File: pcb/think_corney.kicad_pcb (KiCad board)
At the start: 2 copper layers, 130.3 x 86.5 mm, 112 parts

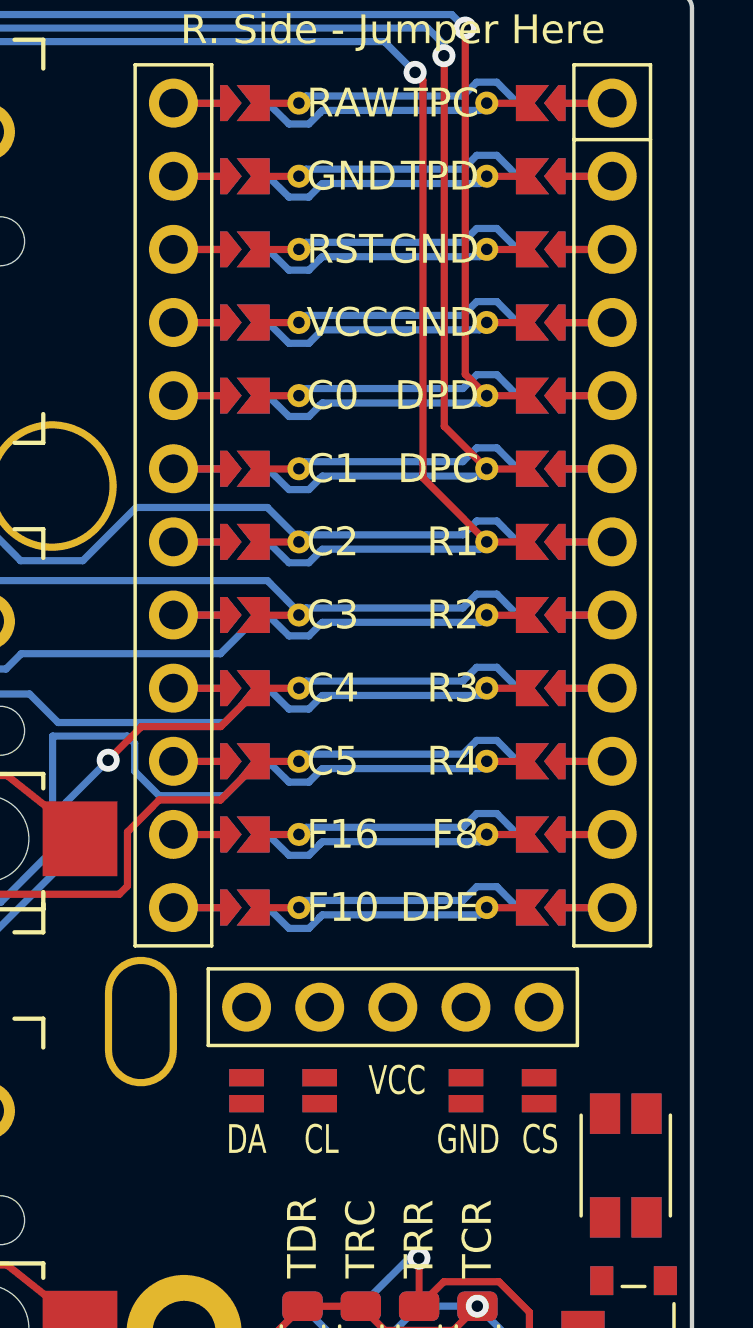
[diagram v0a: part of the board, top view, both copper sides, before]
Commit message: Traces: Added display traces
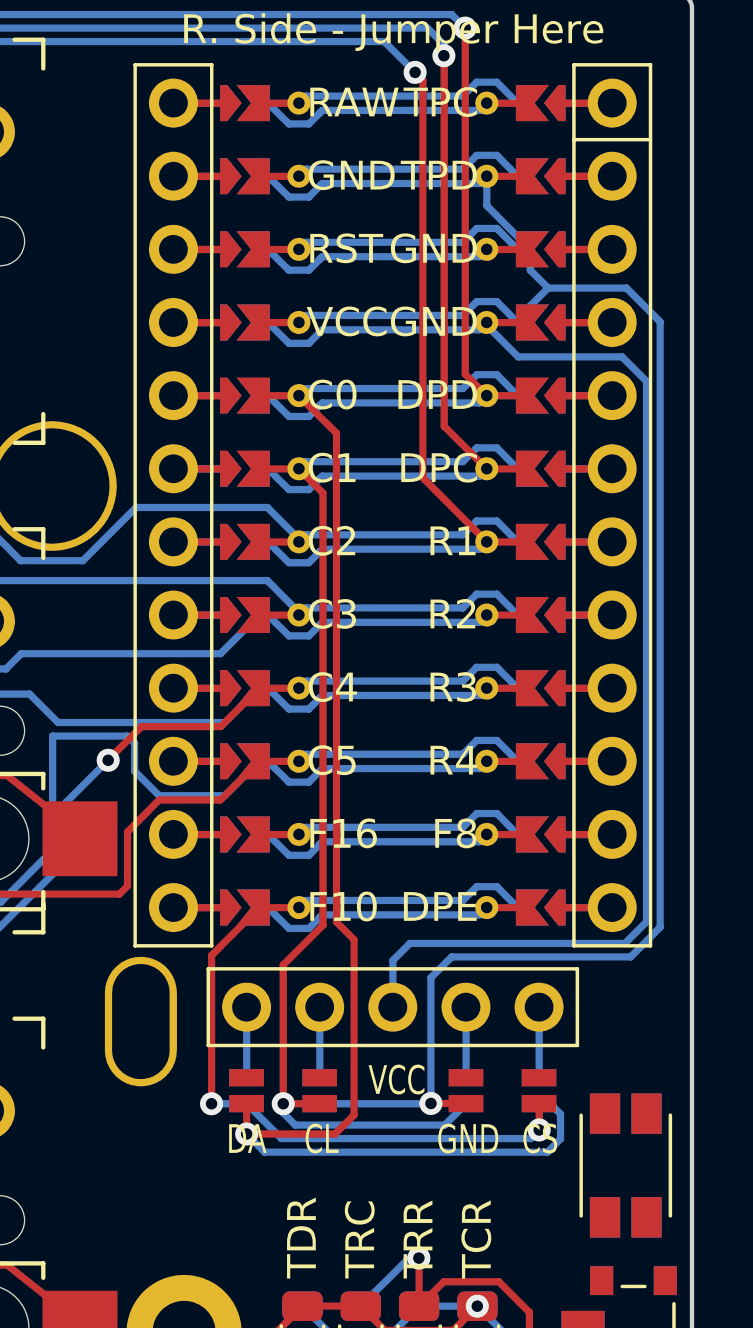
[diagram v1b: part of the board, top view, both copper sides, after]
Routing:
- net GND: track 72.7 -> 122.5 mm, vias 3 -> 4
- net DPD: track 10.2 -> 53.7 mm, vias 0 -> 1
- net VCC: track 45.2 -> 81.3 mm
- net DPC: track 10.2 -> 41.5 mm, vias 0 -> 1
- net DPE: track 10.2 -> 30.4 mm, vias 0 -> 2
- net DISP1_5: track 0.00 -> 2.45 mm
- net DISP1_4: track 0.00 -> 2.45 mm
- net DISP1_2: track 0.00 -> 2.45 mm
- net DISP1_1: track 0.00 -> 2.45 mm

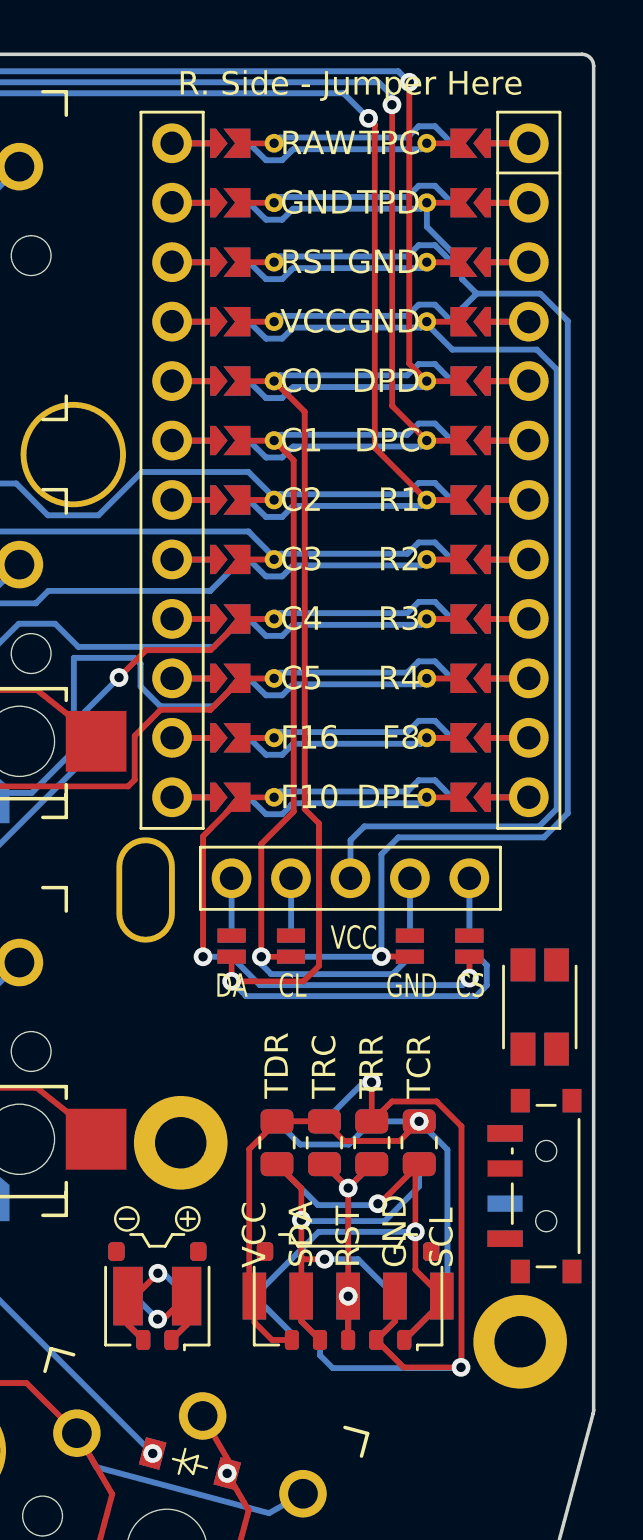
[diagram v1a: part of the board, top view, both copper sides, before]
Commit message: Traces: Added other traces
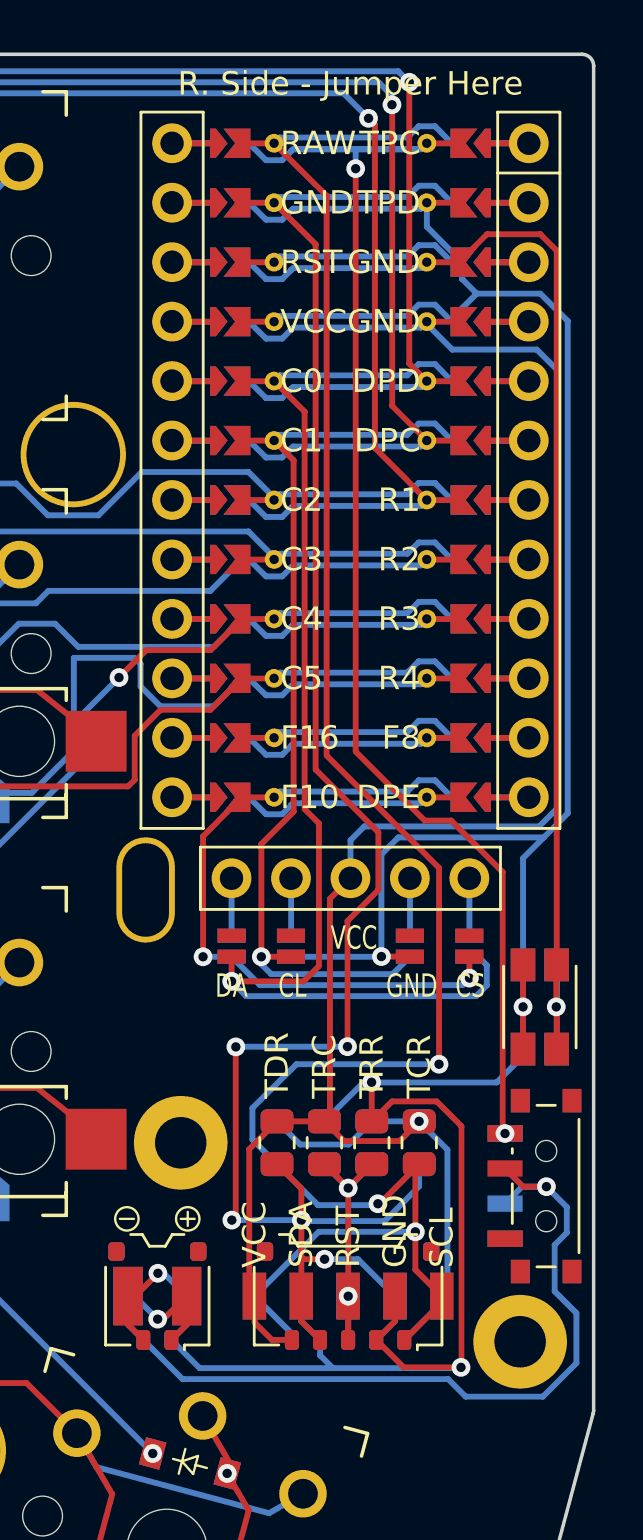
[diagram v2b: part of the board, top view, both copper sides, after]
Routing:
- net TPC: track 36.2 -> 90.0 mm, vias 2 -> 3
- net TPD: track 31.9 -> 85.5 mm, vias 2 -> 5
- net RAW: track 10.1 -> 60.8 mm, vias 0 -> 2
- net RST: track 10.1 -> 52.6 mm, vias 0 -> 1
- net BAT_P: track 7.58 -> 40.3 mm, vias 1 -> 2
- net GND: track 122.5 -> 151.1 mm, vias 4 -> 5
- net VCC: track 81.3 -> 91.8 mm

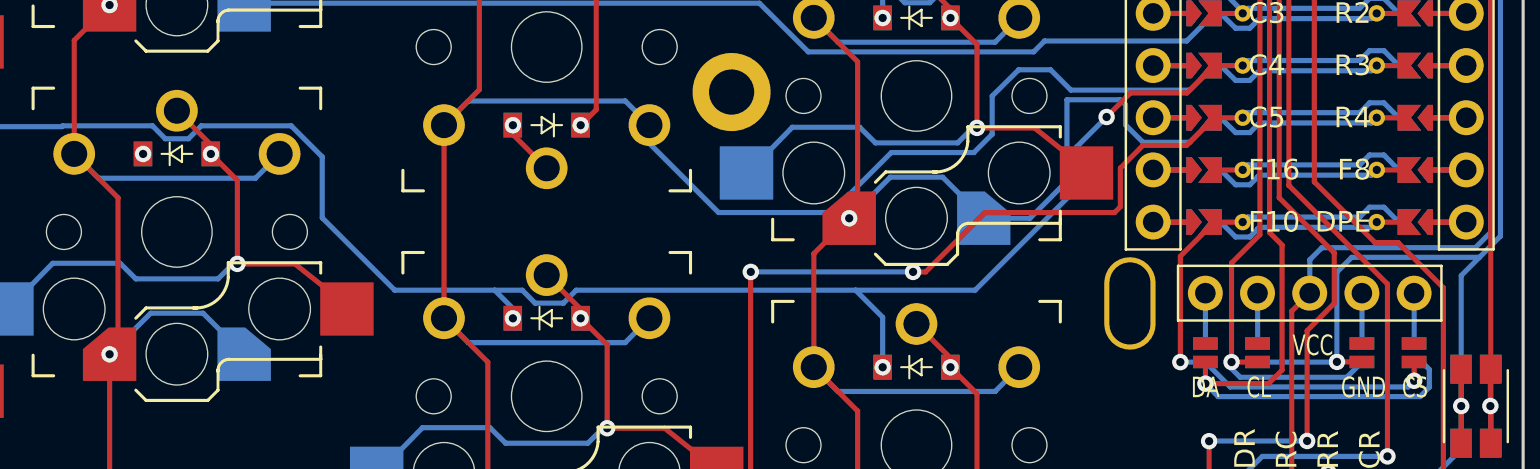
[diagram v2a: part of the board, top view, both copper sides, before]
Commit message: Traces: Added remaining missing traces
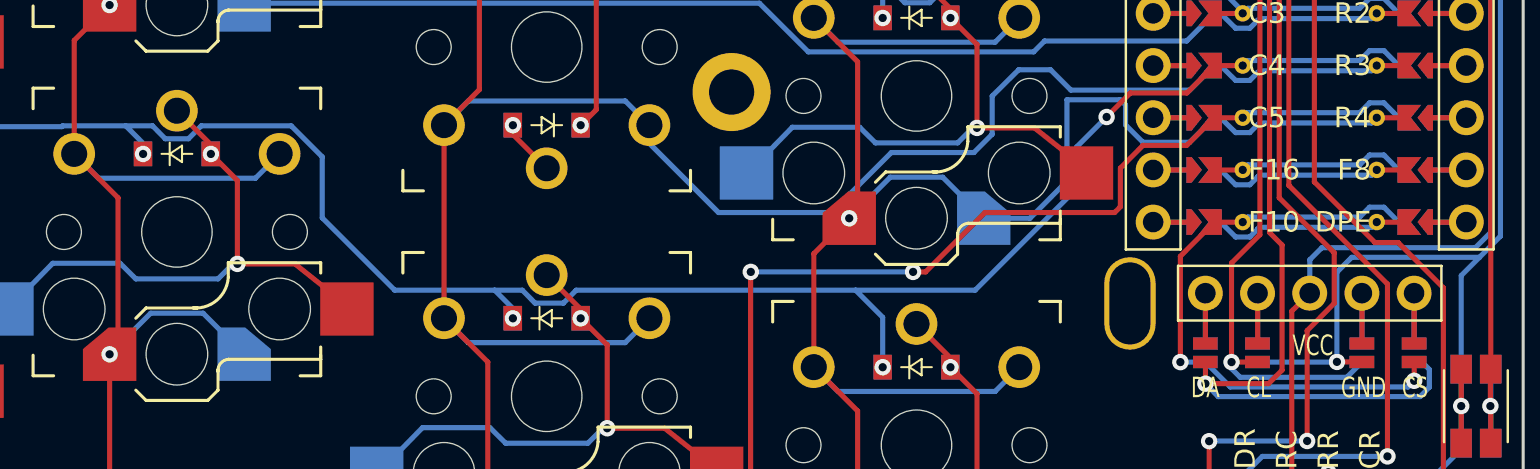
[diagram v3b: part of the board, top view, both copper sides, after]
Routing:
- net DISP1_5: track 2.45 -> 4.90 mm
- net DISP1_4: track 2.45 -> 4.90 mm
- net DISP1_2: track 2.45 -> 4.90 mm
- net DISP1_1: track 2.45 -> 4.90 mm
- net R3: track 169.9 -> 171.1 mm

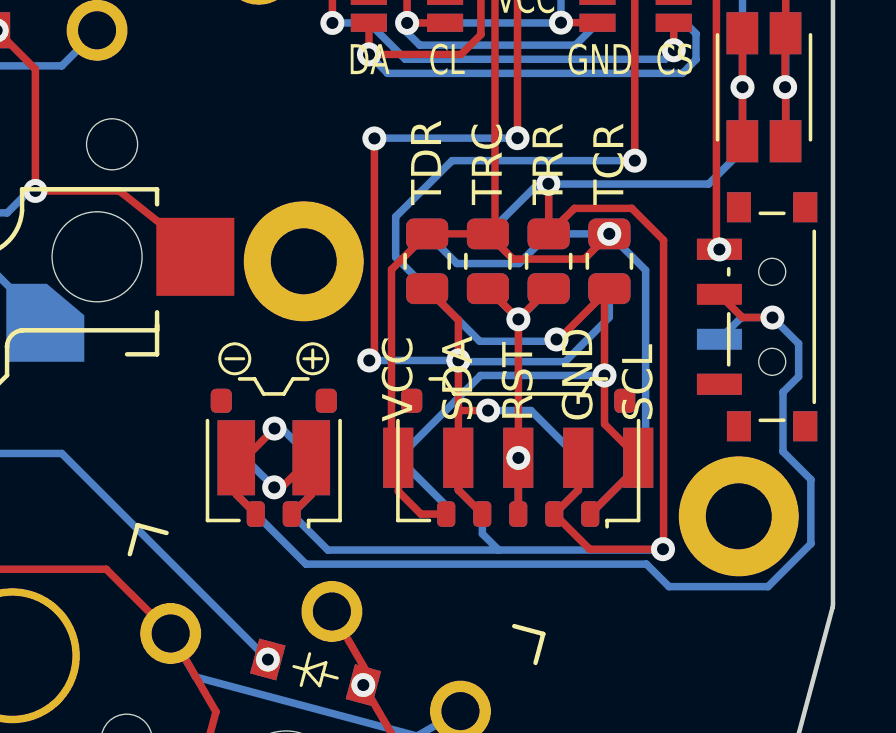
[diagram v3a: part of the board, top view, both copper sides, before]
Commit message: PCB: Submitted test to jlcpcb
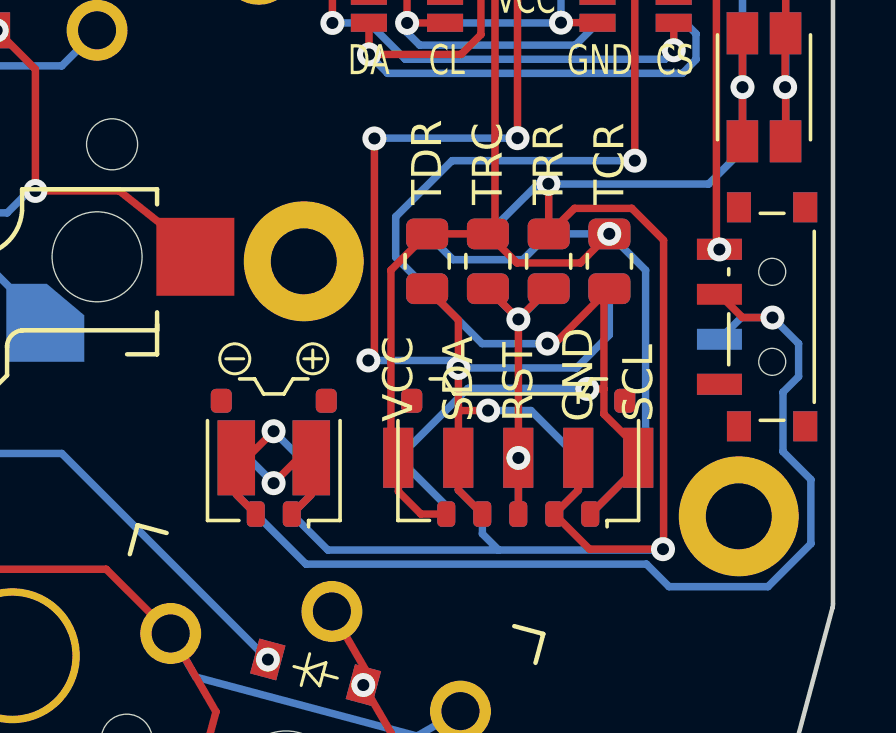
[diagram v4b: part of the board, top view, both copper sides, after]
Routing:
- net BAT_P: track 40.3 -> 37.0 mm
- net GND: track 151.1 -> 147.9 mm
